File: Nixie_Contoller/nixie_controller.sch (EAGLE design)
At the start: 28 parts, among them IC1 DS1307, IC2 7805TV, J1 CON-SOCJ-2155, SW1 EC12E_SW, U1 328P, U2 HU2032-LF, Y2 32.768kHz

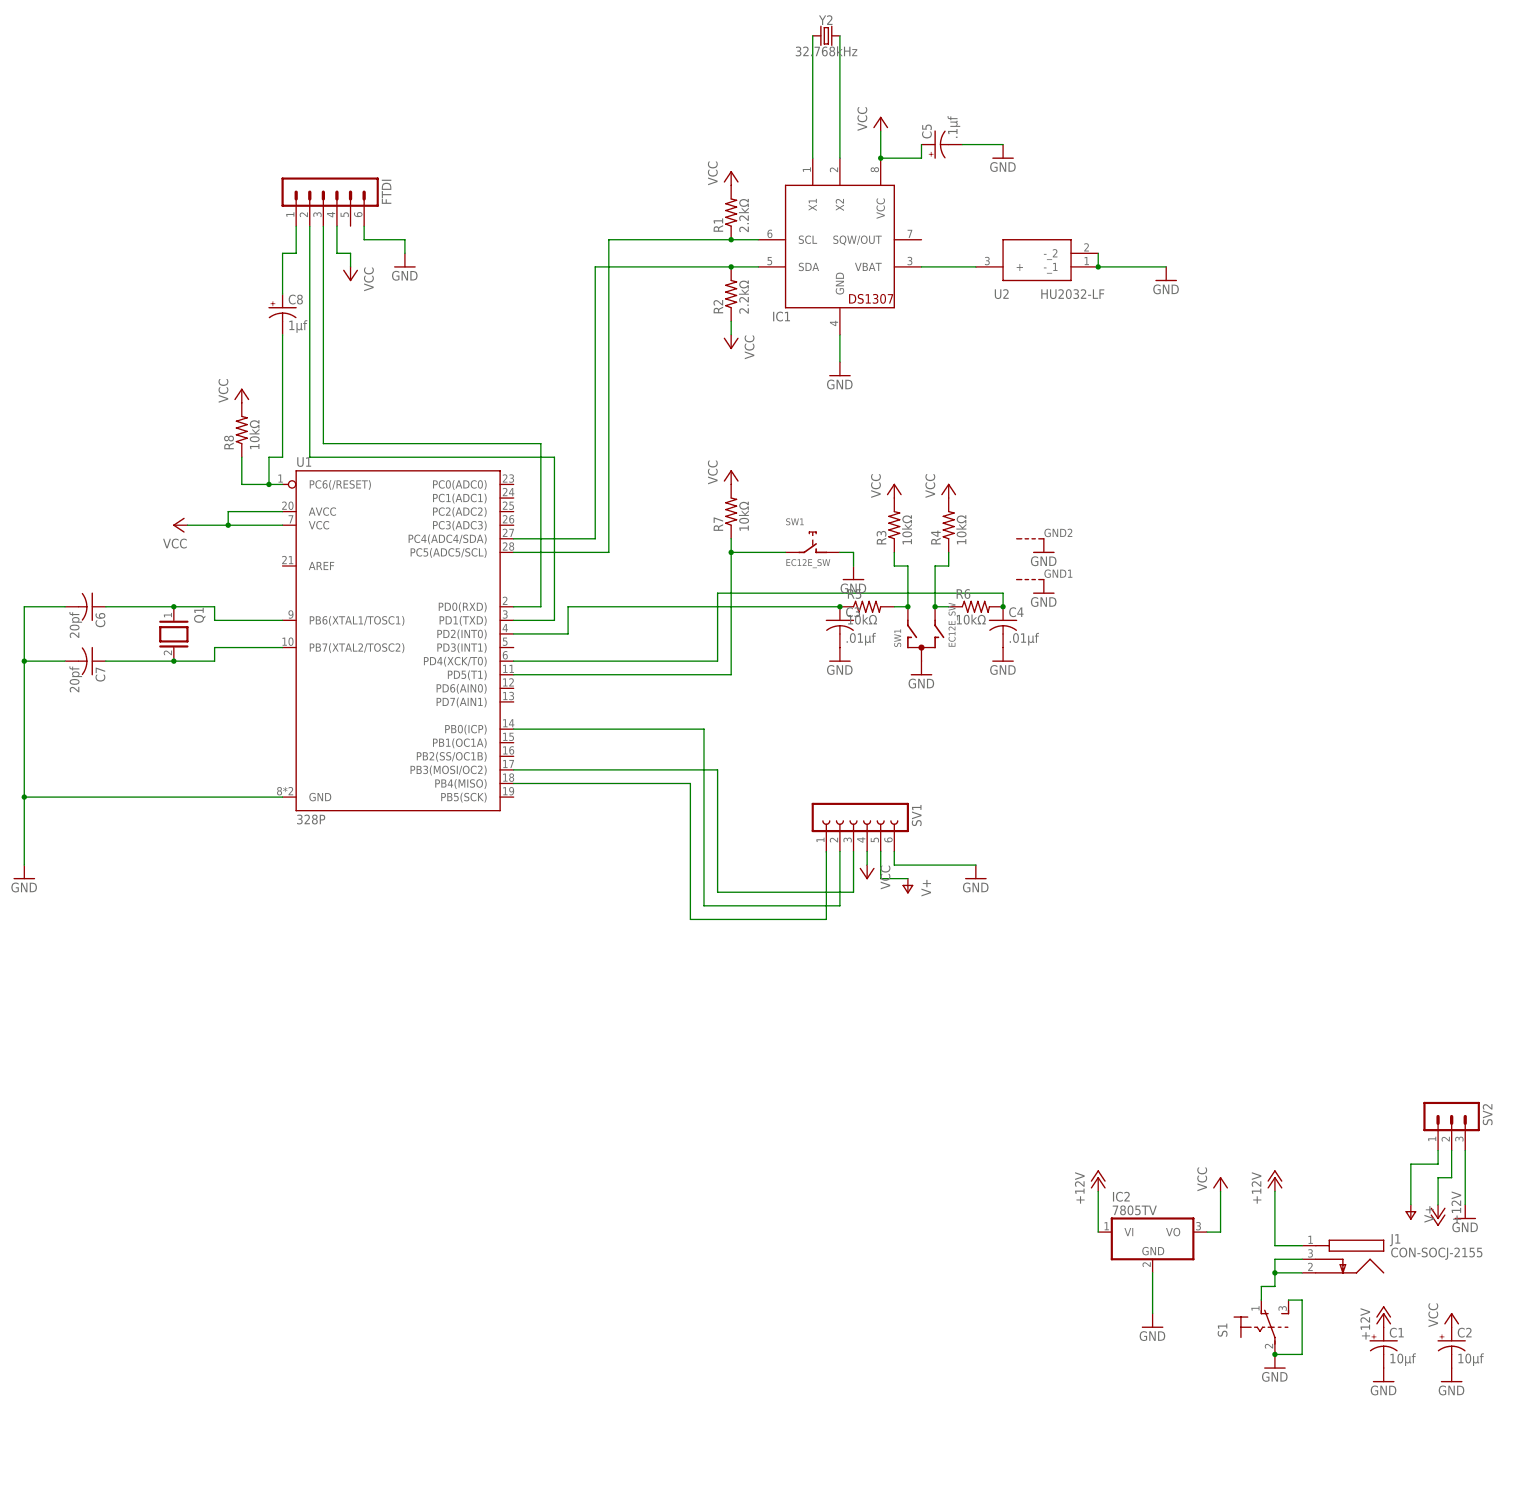
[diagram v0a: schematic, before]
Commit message: Changes to vertical mounted encoder and switch on base
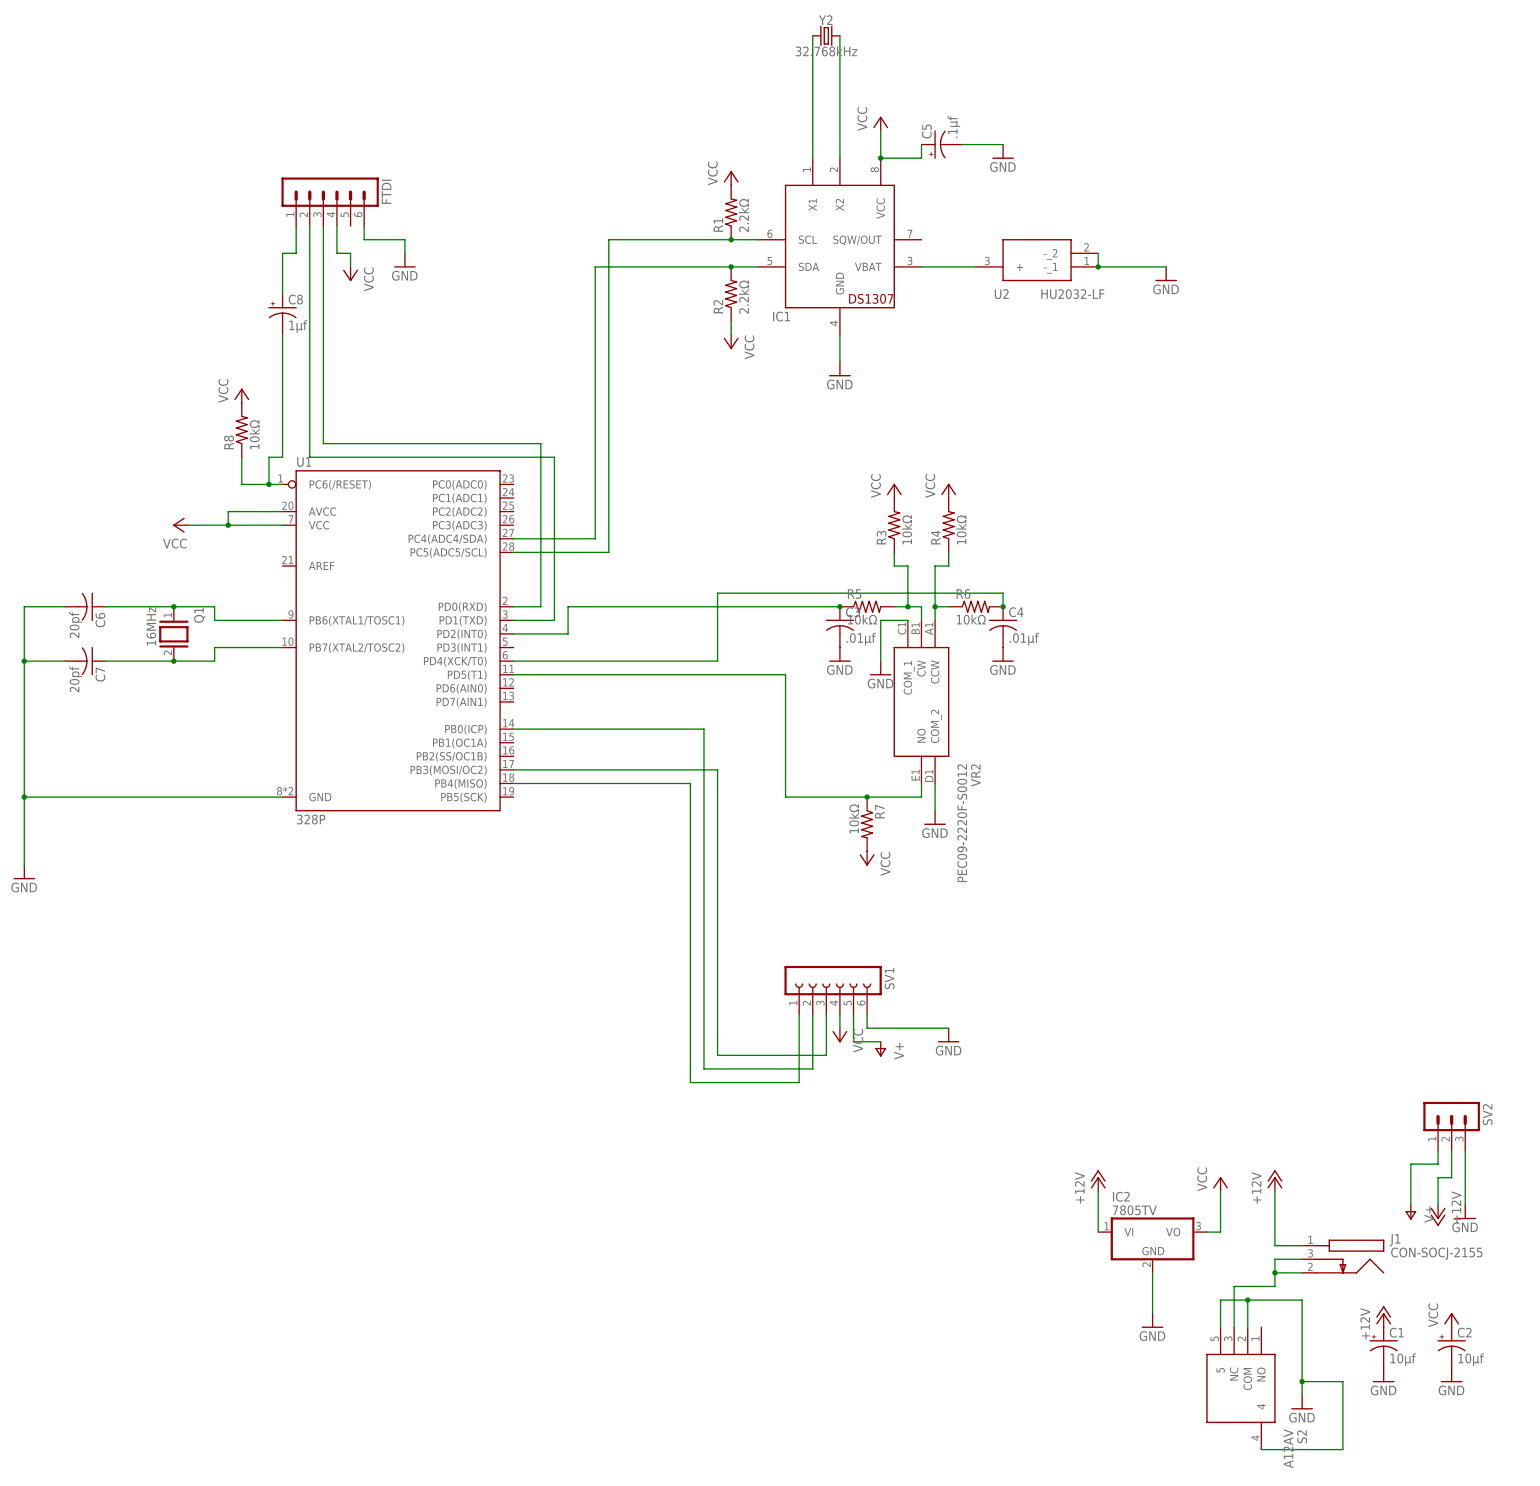
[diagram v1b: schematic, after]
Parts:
- removed S1: (no value), switch:320-938
- removed SW1: EC12E_SW, switch-alps:EC12E_SW
- added S2: A12AV, SamacSys_Parts:A12AV
- added VR2: PEC09-2220F-S0012, SamacSys_Parts:PEC09-2220F-S0012
- Q1: value (none) -> 16MHz
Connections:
- net GND: now also S2.4, S2.5, S2.COM, VR2.COM_1, VR2.COM_2; no longer S11.P, S11.S, SW1G$1.C, SW1G$2.1, SW1G$3.G, SW1G$4.G
- net N$15: now also VR2.CW; no longer SW1G$1.A
- net N$2: now also VR2.NO; no longer SW1G$2.2
- net N$3: now also VR2.CCW; no longer SW1G$1.B
- net N$6: now also S2.NC; no longer S11.O
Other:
- moved on the sheet: R7, SV1

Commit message: small big fixes
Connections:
- net +12V: now also S2.NC; no longer J1.1
- net GND: now also J1.2, J1.3; no longer S2.COM
- net N$6: now also J1.1, S2.COM; no longer J1.2, J1.3, S2.NC
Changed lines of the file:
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@@
 <attribute name="VALUE" x="251.46" y="30.48" size="1.778" layer="96"/>
 </instance>
-<instance part="P+4" gate="1" x="248.92" y="76.2" smashed="yes" grouprefs="POWER">
-<attribute name="VALUE" x="246.38" y="71.12" size="1.778" layer="96" rot="R90"/>
+<instance part="P+4" gate="1" x="241.3" y="60.96" smashed="yes" grouprefs="POWER">
+<attribute name="VALUE" x="238.76" y="55.88" size="1.778" layer="96" rot="R90"/>
 </instance>
 <instance part="P+5" gate="1" x="269.24" y="50.8" smashed="yes" grouprefs="POWER">
@@
 <pinref part="GND3" gate="1" pin="GND"/>
 <wire x1="254" y1="53.34" x2="254" y2="38.1" width="0.1524" layer="91"/>
-<pinref part="S2" gate="G$1" pin="COM"/>
 <wire x1="254" y1="38.1" x2="254" y2="35.56" width="0.1524" layer="91"/>
-<wire x1="243.84" y1="48.26" x2="243.84" y2="53.34" width="0.1524" layer="91"/>
-<wire x1="243.84" y1="53.34" x2="254" y2="53.34" width="0.1524" layer="91"/>
+<wire x1="238.76" y1="53.34" x2="248.92" y2="53.34" width="0.1524" layer="91"/>
 <pinref part="S2" gate="G$1" pin="5"/>
+<wire x1="248.92" y1="53.34" x2="254" y2="53.34" width="0.1524" layer="91"/>
 <wire x1="238.76" y1="48.26" x2="238.76" y2="53.34" width="0.1524" layer="91"/>
-<wire x1="238.76" y1="53.34" x2="243.84" y2="53.34" width="0.1524" layer="91"/>
-<junction x="243.84" y="53.34"/>
 <pinref part="S2" gate="G$1" pin="4"/>
 <wire x1="246.38" y1="25.4" x2="261.62" y2="25.4" width="0.1524" layer="91"/>
@@
 <wire x1="261.62" y1="38.1" x2="254" y2="38.1" width="0.1524" layer="91"/>
 <junction x="254" y="38.1"/>
+<pinref part="J1" gate="G$1" pin="3"/>
+<wire x1="254" y1="60.96" x2="248.92" y2="60.96" width="0.1524" layer="91" grouprefs="POWER"/>
+<wire x1="248.92" y1="60.96" x2="248.92" y2="58.42" width="0.1524" layer="91" grouprefs="POWER"/>
+<pinref part="J1" gate="G$1" pin="2"/>
+<wire x1="254" y1="58.42" x2="248.92" y2="58.42" width="0.1524" layer="91" grouprefs="POWER"/>
+<wire x1="248.92" y1="58.42" x2="248.92" y2="53.34" width="0.1524" layer="91"/>
+<junction x="248.92" y="58.42"/>
+<junction x="248.92" y="53.34"/>
 </segment>
 <segment>
@@
 </segment>
 <segment>
-<pinref part="P+4" gate="1" pin="+12V"/>
-<wire x1="248.92" y1="73.66" x2="248.92" y2="63.5" width="0.1524" layer="91"/>
-<pinref part="J1" gate="G$1" pin="1"/>
-<wire x1="248.92" y1="63.5" x2="254" y2="63.5" width="0.1524" layer="91"/>
-</segment>
-<segment>
 <pinref part="P+17" gate="1" pin="+12V"/>
 <wire x1="279.4" y1="71.12" x2="279.4" y2="76.2" width="0.1524" layer="91" grouprefs="POWER"/>
@@
 <pinref part="SV2" gate="G$1" pin="2"/>
 <wire x1="281.94" y1="76.2" x2="281.94" y2="81.28" width="0.1524" layer="91" grouprefs="POWER"/>
+</segment>
+<segment>
+<pinref part="S2" gate="G$1" pin="NC"/>
+<pinref part="P+4" gate="1" pin="+12V"/>
+<wire x1="241.3" y1="48.26" x2="241.3" y2="58.42" width="0.1524" layer="91"/>
 </segment>
 </net>
@@
 </segment>
 </net>
-<net name="N$6" class="0">
-<segment>
-<pinref part="J1" gate="G$1" pin="3"/>
-<wire x1="254" y1="60.96" x2="248.92" y2="60.96" width="0.1524" layer="91" grouprefs="POWER"/>
-<wire x1="248.92" y1="60.96" x2="248.92" y2="58.42" width="0.1524" layer="91" grouprefs="POWER"/>
-<pinref part="J1" gate="G$1" pin="2"/>
-<wire x1="254" y1="58.42" x2="248.92" y2="58.42" width="0.1524" layer="91" grouprefs="POWER"/>
-<wire x1="248.92" y1="58.42" x2="248.92" y2="55.88" width="0.1524" layer="91"/>
-<junction x="248.92" y="58.42"/>
-<pinref part="S2" gate="G$1" pin="NC"/>
-<wire x1="241.3" y1="48.26" x2="241.3" y2="55.88" width="0.1524" layer="91"/>
-<wire x1="241.3" y1="55.88" x2="248.92" y2="55.88" width="0.1524" layer="91"/>
-</segment>
-</net>
 <net name="N$14" class="0">
 <segment>
@@
 </segment>
 </net>
+<net name="N$6" class="0">
+<segment>
+<pinref part="J1" gate="G$1" pin="1"/>
+<wire x1="254" y1="63.5" x2="243.84" y2="63.5" width="0.1524" layer="91"/>
+<pinref part="S2" gate="G$1" pin="COM"/>
+<wire x1="243.84" y1="63.5" x2="243.84" y2="48.26" width="0.1524" layer="91"/>
+</segment>
+</net>

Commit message: Snapshot 12-23
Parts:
- removed SV2: (no value), con-lstb:MA03-1
- added C10: 100uF,35V, nick:C-POL-EU7343
- added C11, C9: 100n, rcl:C-EUC0805
- added C12: 4u7,250V, nick:C-POL-EU-NICHICON-UJ-12
- added C13: 100n,250V, nick:C-EU-2420
- added C14: 10uF,25V, nick:C-POL-EU7343
- added D1: ES2F, diode:DIODE-SMC
- added IC3: 7805T, linear:7805T
- added L1: 100uH, nick:L-SMT-POWER-B82479
- added R10: 10K, rcl:R-EU_R0805
- added R9: 1M5, rcl:R-EU_R2512
- added RSENSE: 0R050, rcl:R-EU_R2010
- added T1: IRF644PBF, transistor-power:IRF740
- added VR1: 5K, nick:TRIMPOT-3214W
- IC2: value 7805TV -> MAX1771ESA; device linear:7805TV -> nick:MAX1771ESA
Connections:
- new net EXT: IC2.EXT, T1.G
- new net N$19: D1.A, L1.2, T1.D
- new net N$20: C9.1, IC2.REF
- new net N$23: R10.2, VR1.A, VR1.W
- new net N$24: IC2.CS, RSENSE.2, T1.S
- new net N$8: IC2.FB, R9.1, VR1.B
- net +12V: now also C10.+, C11.1, C14.+, IC2.VCC, IC3.VI, L1.1; no longer IC2.VI, SV2.2
- net GND: now also C10.-, C11.2, C12.-, C13.2, C14.-, C9.2, IC2.AGND, IC2.SHDN, IC3.GND, R10.1, RSENSE.1; no longer SV2.3
- net V+: now also C12.+, C13.1, D1.C, R9.2; no longer SV2.1
- net VCC: now also IC3.VO; no longer IC2.VO
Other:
- note added: "9-16V"
- note added: "9-30V"
- note added: "C1 & C5 should be a low ESR type (e.g. AVX TPS series)"
- note added: "C2 & C5 should be sited very close to pin 2 (Vcc) of IC1"
- note added: "C4 should be low ESR (< 3ohms) and rated > 220V"
- note added: "D1 should be an ultra-fast (<50nS) recovery, 1A 220V"
- note added: "High Efficiency (typically 85%) 50mA, 150-220V, Nixie Power Supply"
- note added: "If PWR > 15V, use a seperate supply (e.g. via a 78L12) for Vcc"
- note added: "If you have stability issues, a 100p 250V ceramic cap could be soldered on top of R2"
- note added: "If you only want 25mA output, you can use a 1A inductor for L1 (e.g. a CDRH125-101) and 0R100 for Rsense"
- note added: "Join J1-1 & J1-2 to Vcc (9-16V)"
- note added: "Join J2-1 & J2-2 to GND"
- note added: "L1 should be 2A rated (e.g. EPCOS B82479 series) for 50mA output"
- note added: "Nick de Smith"
- note added: "Note: The physical board layout is critical in order to obtain high efficiency"
- note added: "R2, C4, C6 must be rated at > 220V operating"
- note added: "Rsense MUST be capable of handling at least 2A"
- note added: "T1 should be selected for low Qg, Rdson & Coss."
- note added: "VR1 adjusts Vout between 150V and 220V and should be multi-turn for more accurate adjustment"

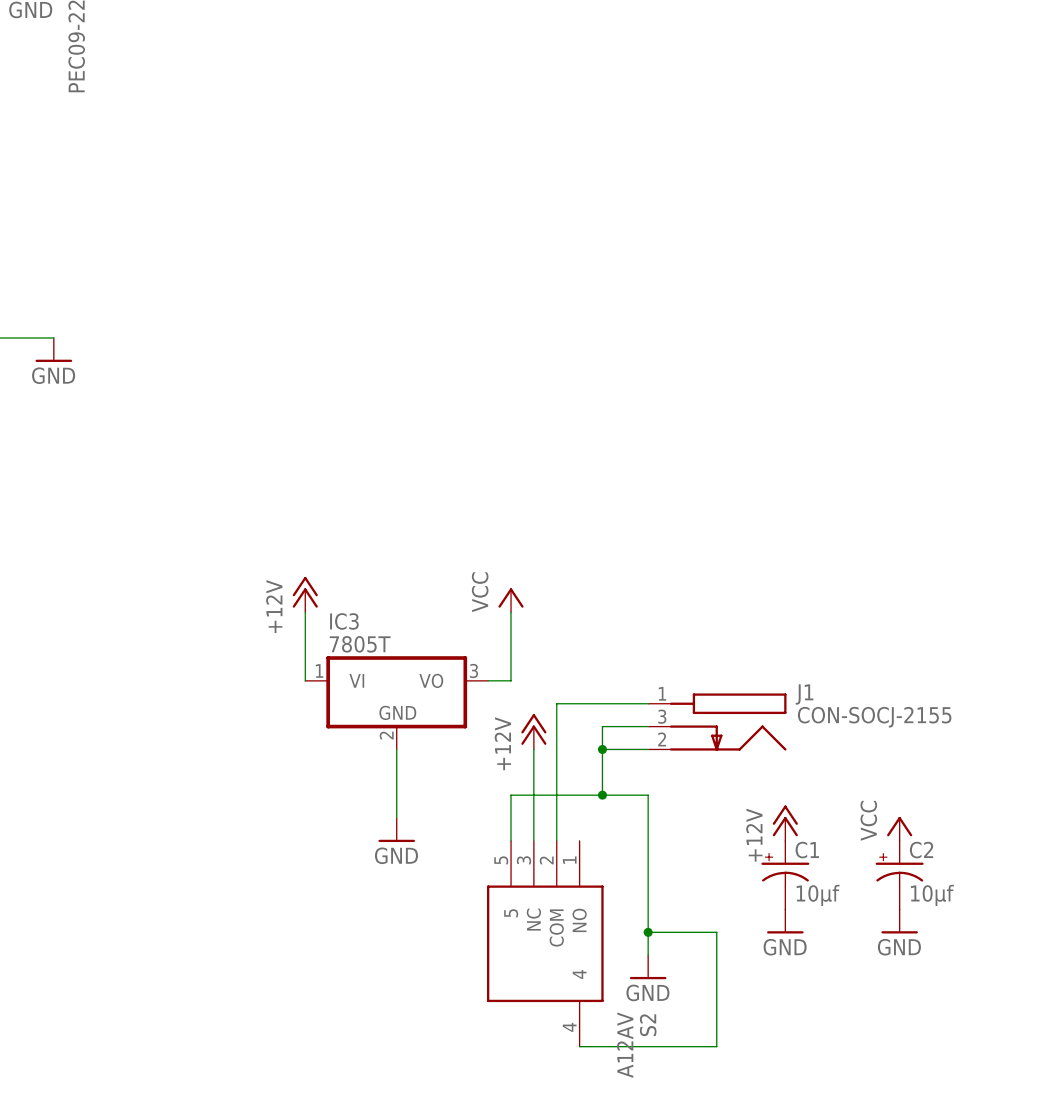
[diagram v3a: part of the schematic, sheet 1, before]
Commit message: Adds LV switching PSU
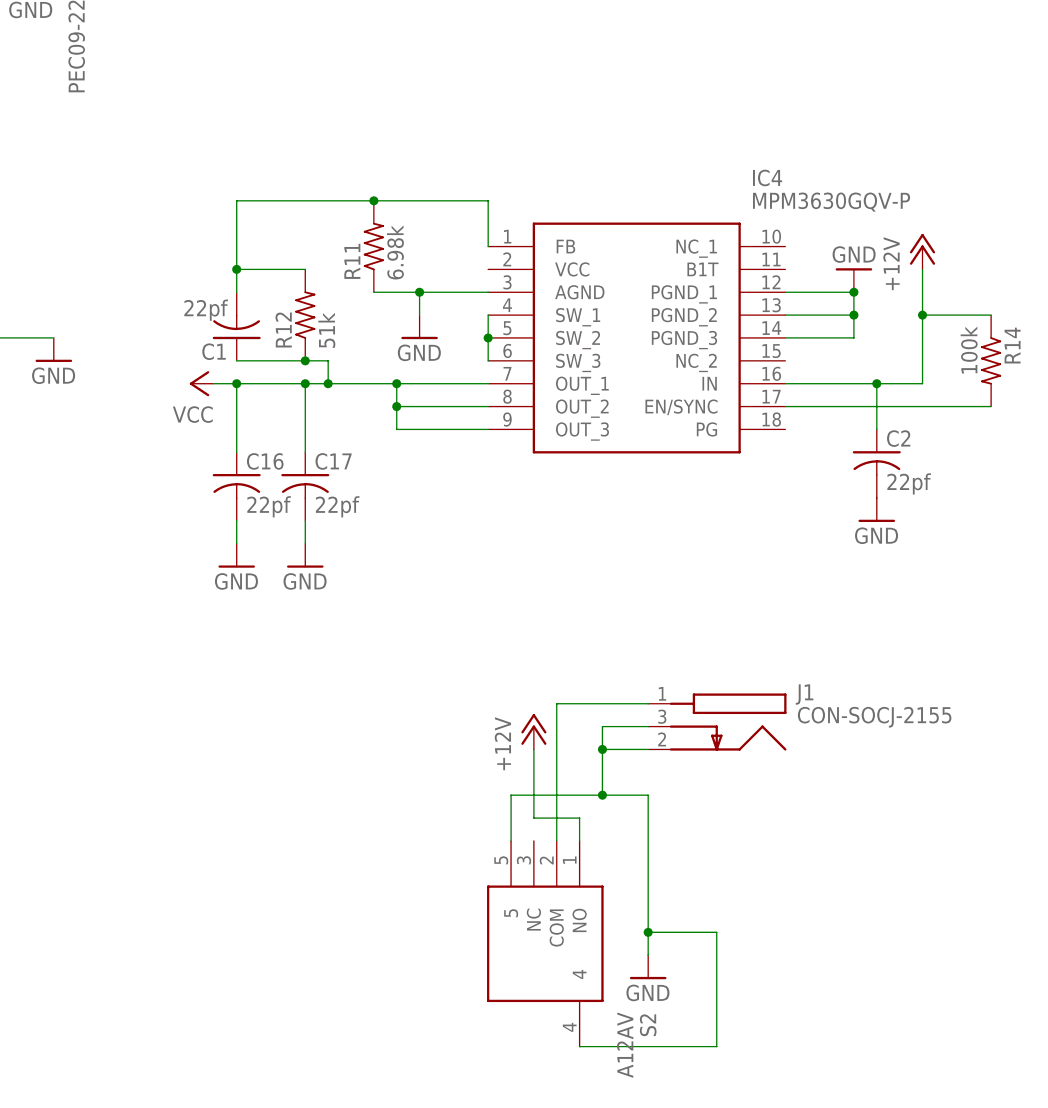
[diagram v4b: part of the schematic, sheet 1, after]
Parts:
- removed IC3: 7805T, linear:7805T
- added C16, C17: 22pf, rcl:C-USC0402
- added IC4: MPM3630GQV-P, SamacSys_Parts:MPM3630GQV-P
- added R11: 6.98k, rcl:R-US_R0201
- added R12: 51k, rcl:R-US_R0201
- added R14: 100k, rcl:R-US_R0201
- C1: value 10μf -> 22pf; device rcl:CPOL-USE2-5 -> rcl:C-USC0201
- C2: value 10μf -> 22pf; device rcl:CPOL-USE2-5 -> rcl:C-USC0603
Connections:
- new net N$25: IC4.SW_1, IC4.SW_2, IC4.SW_3
- new net N$28: IC4.EN/SYNC, R14.2
- new net N$31: C1.2, IC4.FB, R11.2, R12.2
- net +12V: now also C2.1, IC4.IN, R14.1, S2.NO; no longer C1.+, IC3.VI, S2.NC
- net GND: now also C16.2, C17.2, C2.2, IC4.AGND, IC4.PGND_1, IC4.PGND_2, IC4.PGND_3, R11.1; no longer C1.-, C2.-, IC3.GND
- net VCC: now also C1.1, C16.1, C17.1, IC4.OUT_1, IC4.OUT_2, IC4.OUT_3, R12.1; no longer C2.+, IC3.VO
